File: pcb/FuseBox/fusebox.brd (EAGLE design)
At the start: 160 x 100 mm, 49 parts, among them U1 ESP32-DEVKITC-32D, U2 TEXAS_INSTRUMENTS_TPS563249DD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, U3 MAXIM_ELECTRONICS_MAX7221CWGM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, U4 NXP_PCF8574T-3,512NXP_PCF8574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

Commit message: Added some new functions to schematic and layout
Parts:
- added D1: 1N4004, diode:DO41-10
- added Q1: IRF510PbF, transistor-power:TO220BV
- added X3, X5: (no value), con-wago-500:W237-102
- added X4, X6: (no value), con-wago-500:W237-103
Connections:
- removed net GND1: U1.14
- removed net GND2: U1.26
- removed net GND3: U1.20
- new net CS_MAX7219_LEDM: U1.13, X4.1
- new net CS_MAX7221_7SEG: U1.29, U3.12
- new net LASER_SENSE: U1.10
- new net LED_RING: U1.11, X2.2
- new net LOCK_0: Q1.G, U1.12
- new net N$25: D1.A, Q1.D, X5.2
- new net SPI_CLK: U1.28, U3.13, X4.2
- net +12V: now also D1.C, X5.1
- net +3V3: now also X6.3
- net +5V: now also X3.1
- net GND: now also Q1.S, U1.14, U1.20, U1.26, X3.2, X6.1
- net N$23: now also X6.2; no longer X2.2
- net PIEZO_0: now also U1.15; no longer U1.16
- net SPI_MOSI: now also U3.1, X4.3

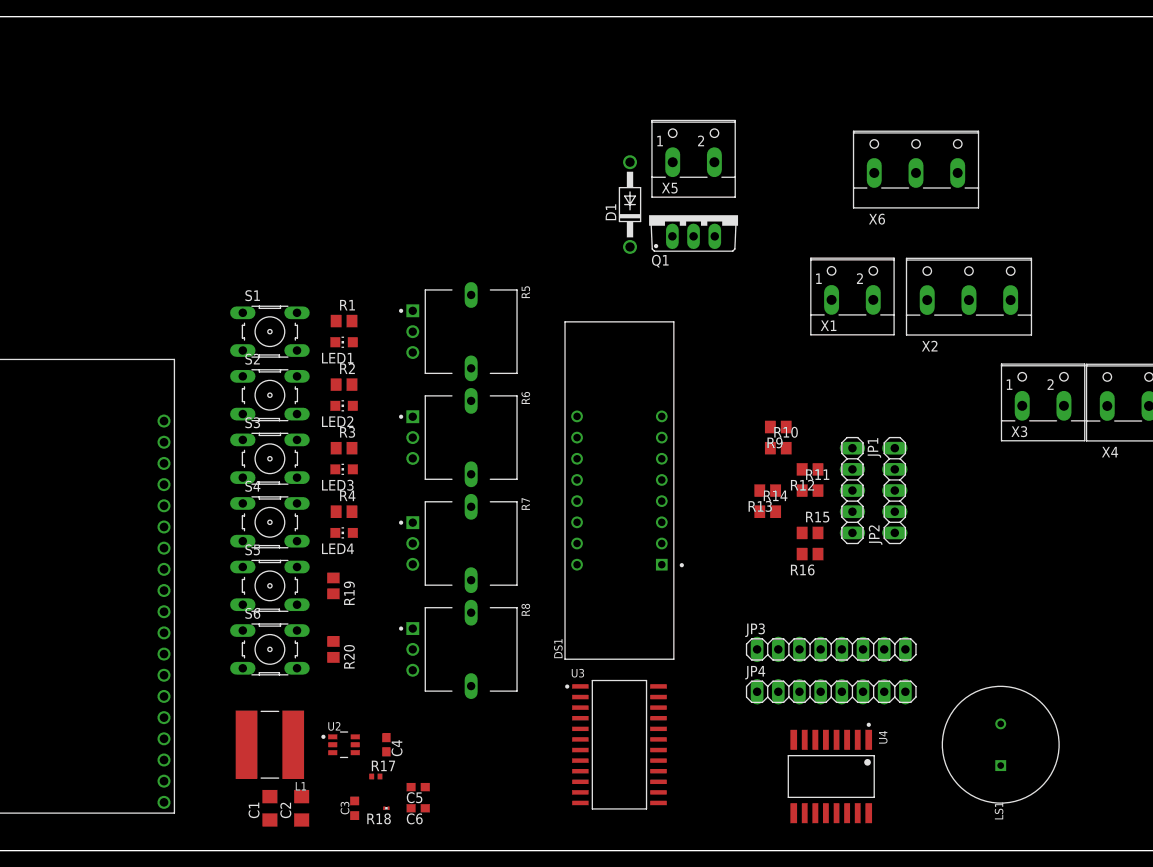
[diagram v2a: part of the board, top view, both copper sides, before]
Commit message: Added second PCF8574 with some buttons and LEDs, finished I2C circuits, finished MAX7221 circuit, rearranged sheets, minor changes in circuit.
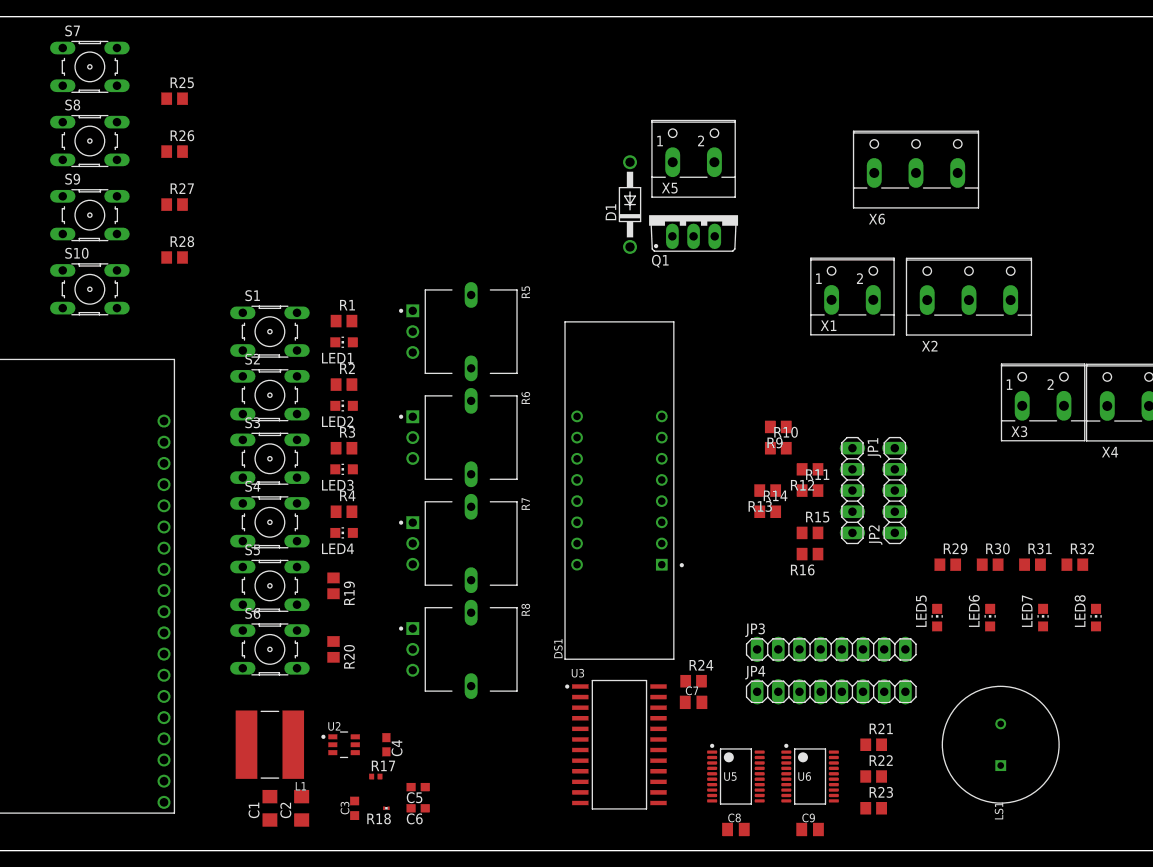
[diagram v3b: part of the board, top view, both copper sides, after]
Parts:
- removed U4: NXP_PCF8574T-3,512NXP_PCF8574T-3,512_0_0, 3,512:NXP_PCF8574T-3,512_0
- added C7, C8, C9: 100n, rcl:C0805K
- added LED5, LED6, LED7, LED8: Red, led:CHIP-LED0805
- added R21, R22, R23, R25, R26, R27, R28: 10k, rcl:R0805
- added R24: 9.53k, rcl:R0805
- added R29, R30, R31, R32: 82, rcl:R0805
- added S10, S7, S8, S9: (no value), switch-omron:B3F-10XX
- added U5, U6: TEXAS_INSTRUMENTS_PCF8574PWTEXAS_INSTRUMENTS_PCF8574PW_0_0, Texas Instruments - PCF8574PW:TEXAS_INSTRUMENTS_PCF8574PW_0
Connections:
- new net BTN_DOWN: S8.3, U6.11
- new net BTN_LEFT: S9.3, U6.12
- new net BTN_RIGHT: S10.3, U6.14
- new net BTN_UP: S7.3, U6.10
- new net DIG_0: DS1.1, U3.2
- new net DIG_1: DS1.2, U3.11
- new net DIG_2: DS1.6, U3.6
- new net DIG_3: DS1.8, U3.7
- new net N$22: R23.1, U5.1, U6.1
- new net N$34: R28.2, S10.4
- new net N$35: LED5.A, R29.1
- new net N$38: LED6.A, R30.1
- new net N$40: LED7.A, R31.1
- new net N$41: LED8.A, R32.1
- new net N$42: LED6.C, U6.17
- new net N$43: LED7.C, U6.19
- new net N$44: LED8.C, U6.20
- net +3V3: now also C8.1, C9.1, R21.2, R22.2, R23.2, R29.2, R30.2, R31.2, R32.2, S10.1, S10.2, S7.1, S7.2, S8.1, S8.2, S9.1, S9.2, U5.5, U6.5, U6.6; no longer U4.16
- net +5V: now also C7.1, R24.2
- net GND: now also C7.2, C8.2, C9.2, R25.1, R26.1, R27.1, R28.1, U5.15, U5.6, U5.7, U5.9, U6.15, U6.7, U6.9; no longer U4.1, U4.2, U4.3, U4.8
- net LASER_SENSE: now also X6.2
- net N$17: now also LED5.C, U6.16; no longer DS1.8, U3.2
- net N$18: now also R25.2, S7.4; no longer DS1.6, U3.11
- net N$19: now also R26.2, S8.4; no longer DS1.2, U3.6
- net N$20: now also R27.2, S9.4; no longer DS1.1, U3.7
- net N$23: now also R24.1, U3.18; no longer X6.2
- net N$26: now also U5.10; no longer U4.4
- net N$27: now also U5.11; no longer U4.5
- net N$28: now also U5.12; no longer U4.6
- net N$29: now also U5.14; no longer U4.7
- net N$30: now also U5.16; no longer U4.9
- net N$31: now also U5.17; no longer U4.10
- net N$32: now also U5.19; no longer U4.11
- net N$33: now also U5.20; no longer U4.12
- net SCL: now also R21.1, U5.2, U6.2; no longer U4.14
- net SDA: now also R22.1, U5.4, U6.4; no longer U4.15

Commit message: Some big changes
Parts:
- removed LED5, LED6, LED7, LED8: Red, led:CHIP-LED0805
- removed R27, R28: 10k, rcl:R0805
- removed R29, R30, R31, R32: 82, rcl:R0805
- removed S10, S7, S8, S9: (no value), switch-omron:B3F-10XX
- removed U6: TEXAS_INSTRUMENTS_PCF8574PWTEXAS_INSTRUMENTS_PCF8574PW_0_0, Texas Instruments - PCF8574PW:TEXAS_INSTRUMENTS_PCF8574PW_0
- added TP1: TPB1,27, testpad:B1,27
- added U$1: NRF52840, Nordic_nRF:AQFN50P700X700X85_HS-74N
- added U4: TEXAS_INSTRUMENTS_ADS1015IDGSTTEXAS_INSTRUMENTS_ADS1015IDGS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, Texas Instruments - ADS1015IDGST:TEXAS_INSTRUMENTS_ADS1015IDGST_0
- R26: value 10k -> 237 1%; device rcl:R0805 -> rcl:0411/15
- S1, S2, S3, S4, S5, S6: value (none) -> MOMENTARY-SWITCH-SPST-SMD-6.2MM-TALL; device switch-omron:B3F-10XX -> SparkFun-Switches:TACTILE_SWITCH_SMD_6.2MM_TALL
- moved R25 134.1 mm to (96.5, -26.5), turned to 90 degrees
- moved R26 125.8 mm to (148.6, 40.6), turned to 90 degrees
- moved C1 102.9 mm to (-57.1, -22.9)
- moved C2 102.9 mm to (-53.3, -22.9)
- moved C3 102.9 mm to (-47.0, -22.9)
- moved C4 102.9 mm to (-43.2, -15.2)
- moved C5 102.9 mm to (-39.4, -20.3)
- moved C6 102.9 mm to (-39.4, -22.9)
- moved R17 102.9 mm to (-44.5, -19.1)
- moved R18 102.9 mm to (-43.2, -22.9)
- moved L1 102.7 mm to (-57.0, -15.0)
- moved U2 102.6 mm to (-48.0, -15.0)
- moved C7 100.1 mm to (-6.00, 1.00)
- moved R24 100.1 mm to (-6.00, 4.00)
- moved U3 99.9 mm to (-15.0, -2.00)
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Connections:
- removed net BTN_DOWN: S8.3, U6.11
- removed net BTN_LEFT: S9.3, U6.12
- removed net BTN_RIGHT: S10.3, U6.14
- removed net BTN_UP: S7.3, U6.10
- removed net N$18: R25.2, S7.4
- removed net N$19: R26.2, S8.4
- removed net N$20: R27.2, S9.4
- removed net N$21: R19.2, S5.4
- removed net N$22: R23.1, U5.1, U6.1
- removed net N$24: R20.2, S6.4
- removed net N$34: R28.2, S10.4
- removed net N$35: LED5.A, R29.1
- removed net N$38: LED6.A, R30.1
- removed net N$40: LED7.A, R31.1
- removed net N$41: LED8.A, R32.1
- removed net N$42: LED6.C, U6.17
- removed net N$43: LED7.C, U6.19
- removed net N$44: LED8.C, U6.20
- new net ADC_RDY: R25.1, U1.32, U4.2
- new net DEC1: U$1.P$C1
- new net DEC4: U$1.P$B5
- new net PCF_INT: R23.1, U1.35, U5.1
- new net VBUS: U$1.P$AD2
- new net VDD: U$1.P$A22, U$1.P$AD14, U$1.P$AD23, U$1.P$B1, U$1.P$W1
- new net VDDH: U$1.P$Y2
- new net VSS: U$1.P$B7
- net +12V: now also TP1.TP
- net +3V3: now also R25.2, S5.B2, S6.B2, U4.8; no longer R29.2, R30.2, R31.2, R32.2, S10.1, S10.2, S5.1, S5.2, S6.1, S6.2, S7.1, S7.2, S8.1, S8.2, S9.1, S9.2, U6.5, U6.6
- net BUTTON_0: now also R19.2, S5.A2; no longer S5.3
- net BUTTON_1: now also R20.2, S6.A2; no longer S6.3
- net GND: now also S1.B2, S2.B2, S3.B2, S4.B2, U4.1, U4.3; no longer R25.1, R26.1, R27.1, R28.1, S1.1, S1.2, S2.1, S2.2, S3.1, S3.2, S4.1, S4.2, U6.15, U6.7, U6.9
- net N$11: now also S4.A2; no longer S4.3, S4.4
- net N$17: now also R26.1, R26.2; no longer LED5.C, U6.16
- net N$5: now also S1.A2; no longer S1.3, S1.4
- net N$7: now also S2.A2; no longer S2.3, S2.4
- net N$9: now also S3.A2; no longer S3.3, S3.4
- net POTI_0: now also U4.4; no longer U1.35
- net POTI_1: now also U4.5; no longer U1.34
- net POTI_2: now also U4.6; no longer U1.33
- net POTI_3: now also U4.7; no longer U1.32
- net SCL: now also U4.10; no longer U6.2
- net SDA: now also U4.9; no longer U6.4
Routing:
- net POTI_1: track 0.00 -> 5.89 mm
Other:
- board text added: "0x58+0x42=0b........?"

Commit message: Further work on PCB
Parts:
- removed U$1: NRF52840, Nordic_nRF:AQFN50P700X700X85_HS-74N
- added C10: 100n, rcl:C0805K
- added F1: MF-SMDF150, fuse:MF-SMDF050
- added LED5, LED6, LED7, LED8: Red, led:CHIP-LED0805
- added R27, R32, R33, R34, R35: 10k, rcl:R0805
- added R28, R29, R30, R31: 82, rcl:R0805
- added S10, S7, S8, S9: MOMENTARY-SWITCH-SPST-SMD-6.2MM-TALL, SparkFun-Switches:TACTILE_SWITCH_SMD_6.2MM_TALL
- added TP10, TP11, TP12, TP13, TP14, TP15, TP16, TP17, TP2, TP3, TP4, TP5, TP6, TP7, TP8, TP9: TPB1,27, testpad:B1,27
- added U6: TEXAS_INSTRUMENTS_PCF8574PWTEXAS_INSTRUMENTS_PCF8574PW_0_0, Texas Instruments - PCF8574PW:TEXAS_INSTRUMENTS_PCF8574PW_0
- moved S6 155.6 mm to (136.0, 15.0)
- moved R20 151.3 mm to (136.0, 9.00), turned to 0 degrees
- moved R8 142.7 mm to (98.0, 77.0), turned to 0 degrees
- moved S5 140.8 mm to (110.0, 15.0)
- moved R19 138.5 mm to (110.0, 9.00), turned to 0 degrees
- moved R7 126.6 mm to (86.0, 77.0), turned to 0 degrees
- moved X6 119.1 mm to (6.99, 19.7), turned to 270 degrees
- moved LED2 114.8 mm to (28.0, 86.0)
- moved LED3 114.7 mm to (28.0, 78.0)
- moved R2 114.7 mm to (28.0, 88.0)
- moved LED4 114.7 mm to (28.0, 70.0)
- moved R3 114.7 mm to (28.0, 80.0)
- moved R4 114.7 mm to (28.0, 72.0)
- moved LED1 114.5 mm to (28.0, 94.0)
- moved R1 114.5 mm to (28.0, 96.0)
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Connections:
- net N$10 renamed SEG_C
- net N$12 renamed SEG_D
- net N$13 renamed SEG_DP
- net N$14 renamed SEG_E
- net N$15 renamed SEG_F
- net N$16 renamed SEG_G
- net N$6 renamed SEG_A
- net N$8 renamed SEG_B
- removed net DEC1: U$1.P$C1
- removed net DEC4: U$1.P$B5
- removed net PCF_INT: R23.1, U1.35, U5.1
- removed net VBUS: U$1.P$AD2
- removed net VDD: U$1.P$A22, U$1.P$AD14, U$1.P$AD23, U$1.P$B1, U$1.P$W1
- removed net VDDH: U$1.P$Y2
- removed net VSS: U$1.P$B7
- new net N$18: C1.1, C2.1, C3.1, F1.2, TP1.TP, U2.3, U2.5
- new net N$19: LED5.C, U6.10
- new net N$20: LED6.A, R29.1
- new net N$21: LED6.C, U6.11
- new net N$22: LED7.A, R30.1
- new net N$24: LED7.C, U6.12
- new net N$34: LED8.A, R31.1
- new net N$35: LED8.C, U6.14
- new net P4_BTN7: R32.2, S7.A2, U6.16
- new net P5_BTN8: R33.2, S8.A2, U6.17
- new net P6_BTN9: R34.2, S9.A2, U6.19
- new net P7_BTN10: R35.2, S10.A2, U6.20
- new net PCF_INT_0: R23.1, TP16.TP, U1.4, U5.1
- new net PCF_INT_1: R27.1, TP15.TP, U1.3, U6.1
- net +0V9: now also TP5.TP
- net +12V: now also F1.1; no longer C1.1, C2.1, C3.1, TP1.TP, U2.3, U2.5
- net +1V5: now also TP4.TP
- net +2V1: now also TP3.TP
- net +2V7: now also TP2.TP
- net +3V3: now also C10.1, R27.2, R28.2, R29.2, R30.2, R31.2, S10.B2, S7.B2, S8.B2, S9.B2, U6.5, U6.6
- net +5V: now also TP6.TP
- net ADC_RDY: now also TP14.TP
- net CS_MAX7219_LEDM: now also TP17.TP
- net CS_MAX7221_7SEG: now also TP13.TP
- net GND: now also C10.2, R26.1, R26.2, R32.1, R33.1, R34.1, R35.1, TP7.TP, U6.15, U6.7, U6.9
- net N$17: now also LED5.A, R28.1; no longer R26.1, R26.2
- net N$39: now also TP8.TP
- net SCL: now also TP10.TP, U6.2
- net SDA: now also TP11.TP, U6.4
- net SPI_CLK: now also TP9.TP
- net SPI_MOSI: now also TP12.TP
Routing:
- net +5V: track 0.00 -> 50.5 mm, vias 0 -> 2
- net SEG_DP: track 0.00 -> 48.9 mm, vias 0 -> 1
- net DIG_3: track 0.00 -> 45.5 mm, vias 0 -> 1
- net SEG_C: track 0.00 -> 43.0 mm, vias 0 -> 1
- net SEG_E: track 0.00 -> 43.0 mm, vias 0 -> 1
- net DIG_2: track 0.00 -> 42.1 mm, vias 0 -> 1
- net SEG_D: track 0.00 -> 40.8 mm, vias 0 -> 1
- net SEG_F: track 0.00 -> 36.8 mm, vias 0 -> 1
- net DIG_0: track 0.00 -> 35.2 mm, vias 0 -> 1
- net SEG_G: track 0.00 -> 30.0 mm, vias 0 -> 1
- net SEG_A: track 0.00 -> 28.3 mm, vias 0 -> 1
- net SEG_B: track 0.00 -> 26.5 mm, vias 0 -> 1
- net DIG_1: track 0.00 -> 25.9 mm, vias 0 -> 1
- net +3V3: track 0.00 -> 23.6 mm, vias 0 -> 13
- net POTI_0: track 0.00 -> 22.2 mm, vias 0 -> 1
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- added copper zone on layer 15, net +3V3
- added copper zone on layer 1, net +5V
- added copper zone on layer 1, net GND
- added copper zone on layer 2, net GND
- added copper zone on layer 1, net N$18
- added copper zone on layer 1, net N$37
